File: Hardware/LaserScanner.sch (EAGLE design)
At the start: 88 parts, among them J1 USB, J2 !KILL!, J3 KEYSWITCH, J5 ESTOP, J8 Power Input, Q1 MBT3904DW1T1, Q4 2.5A/30V/105mΩ, U1 ESP-WROOM-32, U2 3.3V, U3 CH340C

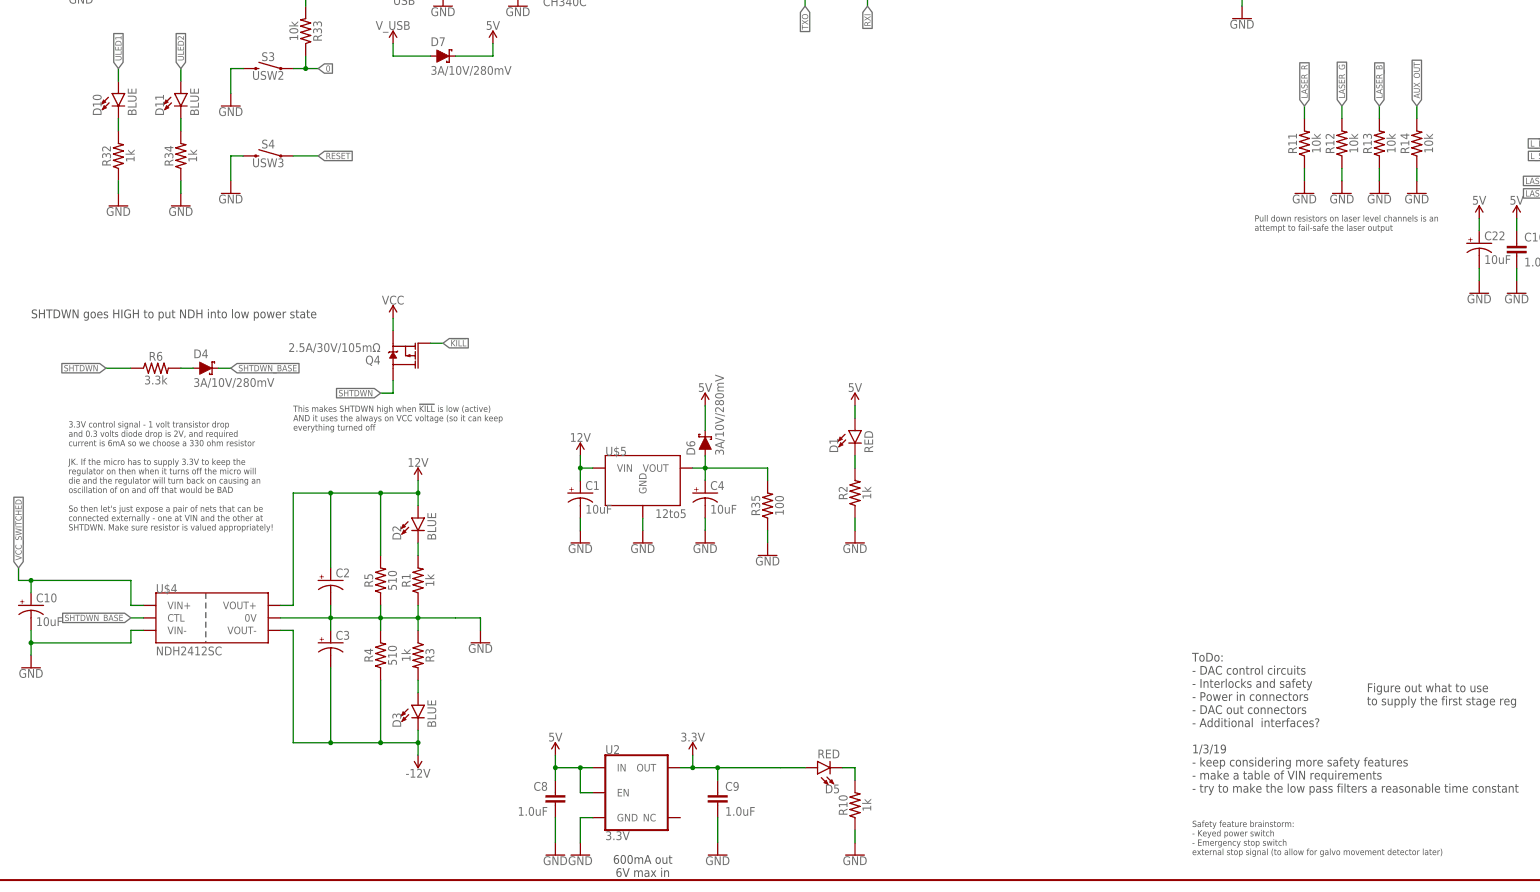
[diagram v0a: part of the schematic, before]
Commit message: add failsafes to schematic
failsafes include:
- pulling the laser dac clr line to gnd if kill_n goes low or if VCC is interrupted (can be used to safe the laser)
- disabling the 3.3V rail (effectively stopping laser output and microcontroller) when kill_n or VCC go low (allowing external kill and interlocks to make safe even when USB is powering 5V rail)

todo: routing
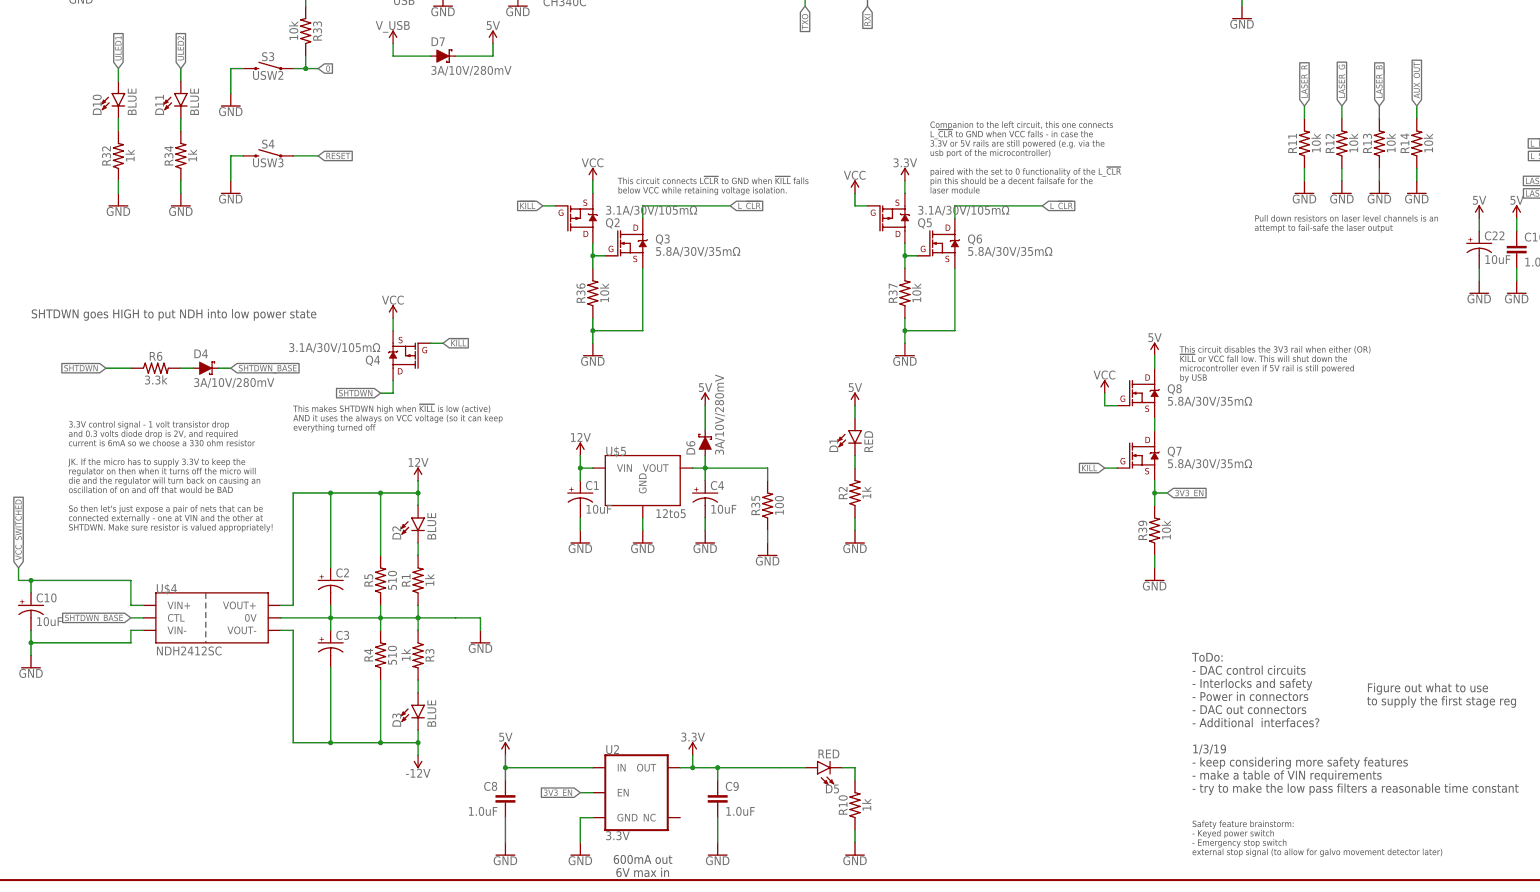
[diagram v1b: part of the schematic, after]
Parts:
- added Q2, Q5: 3.1A/30V/105mΩ, SparkFun-DiscreteSemi:MOSFET_PCH-DMG2307L
- added Q3, Q6, Q7, Q8: 5.8A/30V/35mΩ, SparkFun-DiscreteSemi:MOSFET-NCH-AO3404A
- added R36, R37, R39: 10k, SparkFun-Resistors:10KOHM-0603-1/10W-1%
- Q4: value 2.5A/30V/105mΩ -> 3.1A/30V/105mΩ
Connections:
- new net 3V3_EN: Q7.S, R39.2, U2.EN
- new net N$19: Q2.D, Q3.G, R36.2
- new net N$20: Q5.D, Q6.G, R37.2
- new net N$21: Q7.D, Q8.S
- net !KILL: now also Q2.G, Q7.G
- net 3.3V: now also Q5.S
- net 5V: now also Q8.D; no longer U2.EN
- net GND: now also Q3.S, Q6.S, R36.1, R37.1, R39.1
- net L_!CLR: now also Q3.D, Q6.D
- net VCC: now also Q2.S, Q5.G, Q8.G
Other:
- note added: "Companion to the left circuit, this one connects L_!CLR! to GND when VCC falls - in case the 3.3V or 5V rails are still powered (e.g. via the usb port of the microcontroller) paired with the set to 0 functionality of the L_!CLR! pin this should be a decent failsafe for the laser module"
- note added: "This circuit connects L!CLR! to GND when !KILL! falls below VCC while retaining voltage isolation."
- note added: "This circuit disables the 3V3 rail when either (OR) !KILL! or VCC fall low. This will shut down the microcontroller even if 5V rail is still powered by USB"
- moved on the sheet: C8
